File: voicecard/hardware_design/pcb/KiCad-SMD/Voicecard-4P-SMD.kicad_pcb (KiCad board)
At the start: 2 copper layers, 118.7 x 60.3 mm, 92 parts, among them IC1 TL074P, IC2 LM13700N, IC3 TL072P, IC4 V2164D, IC5 TL072P, IC6 MCP4822, IC7 ATMega328p, Q1 2N3906, Q2 2N3906, Q3 20MHz

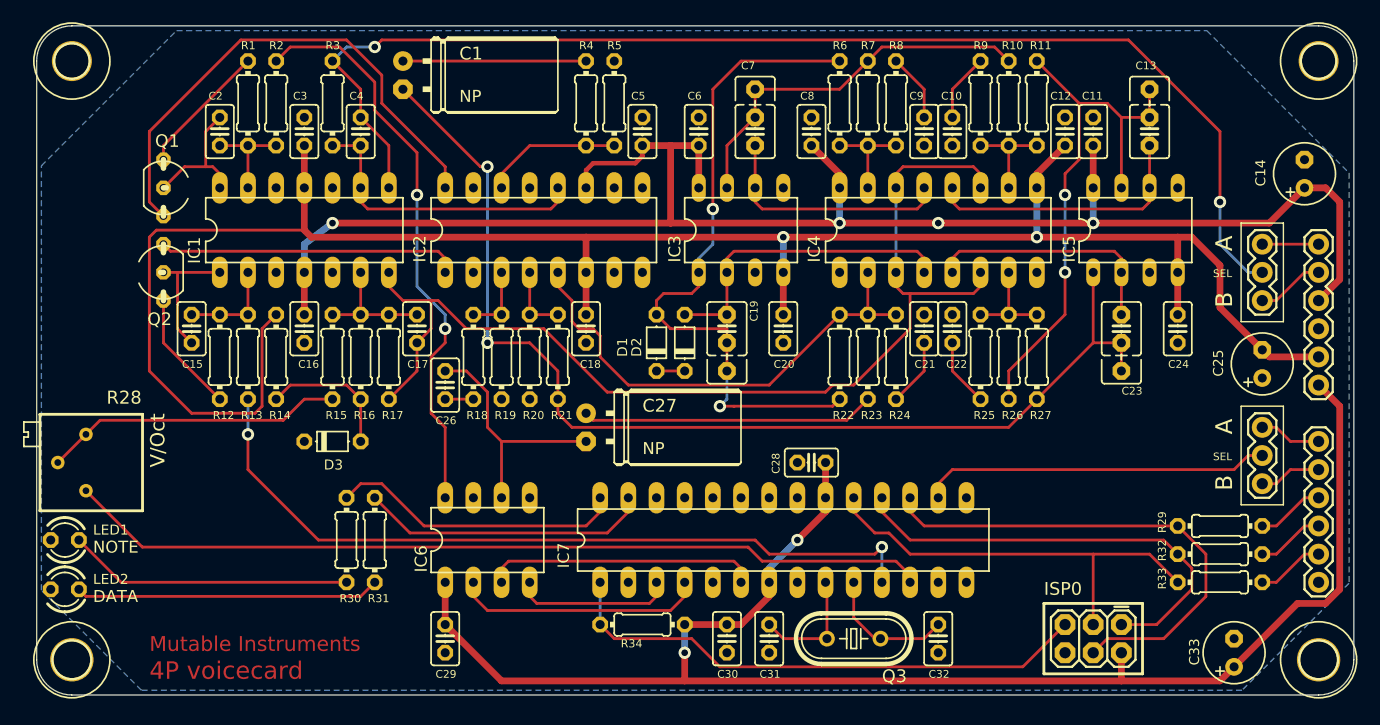
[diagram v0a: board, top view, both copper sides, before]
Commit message: Voicecard 4P SMD: update the board from the schematic and prepare for placement
Footprints replaced in place: every footprint now the schematic's SMD one,
sitting at its through-hole predecessor's position, orientation and layer,
keeping its schematic path. kicad-cli has no update-from-schematic command and
pcbnew does not wrap BOARD_NETLIST_UPDATER, so this was done explicitly
through pcbnew and then checked against the schematic netlist: 92 footprints
(81 replaced, 5 board-only, 6 kept through-hole), 277 of 277 pad nets matching
with nothing extra or missing, and the same net set as the schematic. IC2 pads
7-10 carry no net, being the LM13700 buffer half the 4P does not use.

All 445 track segments, including 20 vias, and the single GND zone are gone.
The Edge.Cuts outline, the four mounting holes, JP1-JP4 and ISP0 are locked:
the motherboard fixes them.

Design rules set to JLCPCB 2-layer standard in the project file: 0.127 mm
minimum track and clearance, 0.3 mm minimum via drill, 0.6 mm minimum via
diameter. Net classes: Default at 0.2 mm track, and a new Power class at
0.4 mm carrying +5V, VCC, VEE and GND. The .kicad_pro is JSON and was edited
with the json module.

DRC reports 196 unconnected items, which is the point of this state, plus one
copper_edge_clearance error where C33's pad crosses the board edge because the
6.3 mm electrolytic sits where a smaller can sat; it goes when C33 is placed.
The 57 warnings are silkscreen and text-height noise inherited from the Eagle
import, along with 4 library mismatches on the imported mounting holes; the
untouched KiCad/ baseline reports 205 violations of the same kinds.

Nothing is placed and nothing is routed.

Co-Authored-By: Claude Opus 5 (1M context) <noreply@anthropic.com>
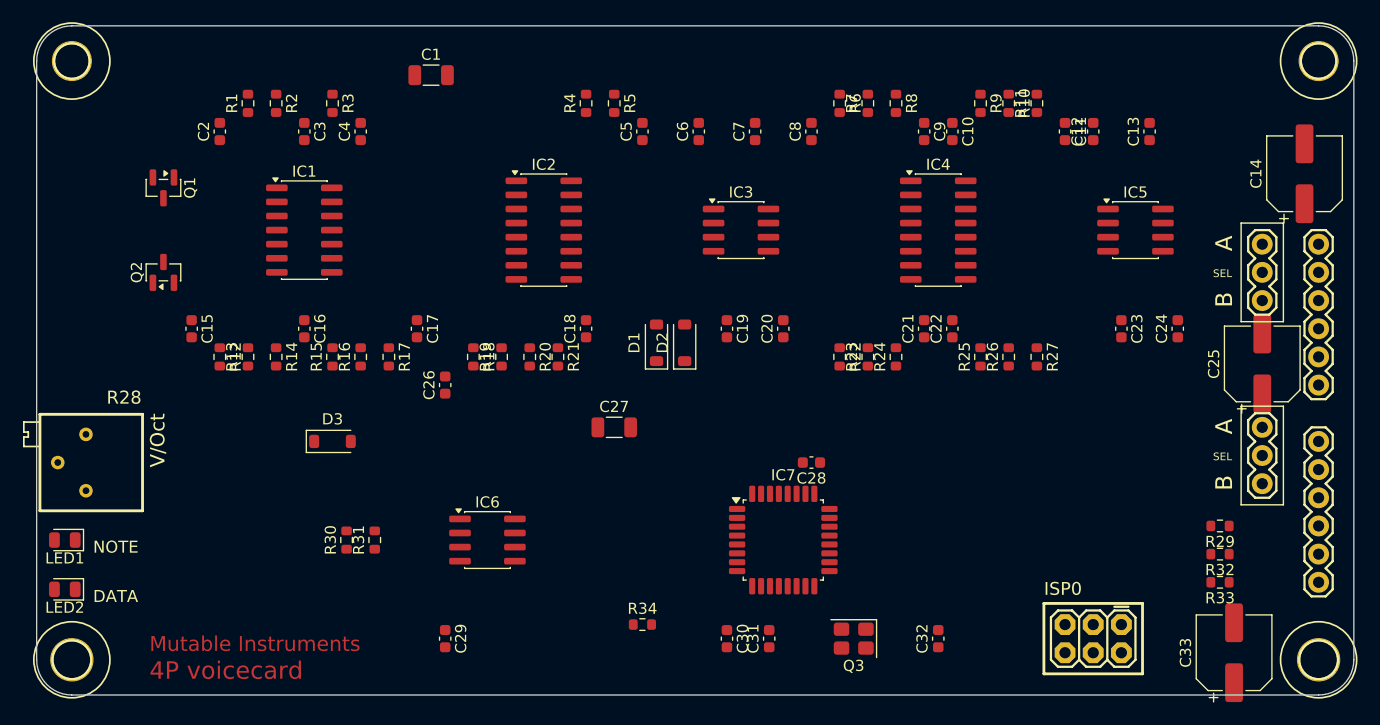
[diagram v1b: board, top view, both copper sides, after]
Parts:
- C1, C27: footprint Voicecard-4P-v01-import-fps:ENP11-6.3 -> Capacitor_SMD:C_1206_3216Metric
- C10, C11, C12, C15, C16, C17, C18, C2, C20, C21, C22, C24, C26, C28, C29, C3, C30, C31, C32, C4, C5, C6, C8, C9: footprint Voicecard-4P-v01-import-fps:C025-025X050 -> Capacitor_SMD:C_0603_1608Metric
- C13, C19, C23, C7: footprint Voicecard-4P-v01-import-fps:C2.5_5-4 -> Capacitor_SMD:C_0603_1608Metric
- C14, C25, C33: footprint Voicecard-4P-v01-import-fps:E2,5-6 -> Capacitor_SMD:CP_Elec_6.3x7.7
- D1, D2, D3: footprint Voicecard-4P-v01-import-fps:D-5 -> Diode_SMD:D_SOD-123
- IC1: footprint Voicecard-4P-v01-import-fps:DIL14 -> Package_SO:SOIC-14_3.9x8.7mm_P1.27mm
- IC2, IC4: footprint Voicecard-4P-v01-import-fps:DIL16 -> Package_SO:SOIC-16_3.9x9.9mm_P1.27mm
- IC3, IC5, IC6: footprint Voicecard-4P-v01-import-fps:DIL08 -> Package_SO:SOIC-8_3.9x4.9mm_P1.27mm
- IC7: footprint Voicecard-4P-v01-import-fps:DIL28-3 -> Package_QFP:TQFP-32_7x7mm_P0.8mm
- LED1, LED2: footprint Voicecard-4P-v01-import-fps:LED3MM -> LED_SMD:LED_0805_2012Metric
- Q1, Q2: footprint Voicecard-4P-v01-import-fps:TO92- -> Package_TO_SOT_SMD:SOT-23
- Q3: footprint Voicecard-4P-v01-import-fps:HC49U-V -> Crystal:Crystal_SMD_3225-4Pin_3.2x2.5mm
- R1, R10, R11, R12, R13, R14, R15, R16, R17, R18, R19, R2, R20, R21, R22, R23, R24, R25, R26, R27, R29, R3, R30, R31, R32, R33, R34, R4, R5, R6, R7, R8, R9: footprint Voicecard-4P-v01-import-fps:0204_7 -> Resistor_SMD:R_0603_1608Metric
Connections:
- C19 pad 1: Net-(IC3A--IN) -> Net-(D2-A)
- IC3 pad 2: Net-(IC3A--IN) -> Net-(D2-A)
- IC4 pad 4: Net-(IC3A--IN) -> Net-(D2-A)
- IC7 pad 1: Net-(IC7-PC6(/RESET)) -> unconnected-(IC7-PD3(INT1)-Pad1)
- IC7 pad 10: Net-(IC7-PB7(XTAL2/TOSC2)) -> F_PWM
- IC7 pad 11: RES_PWM -> unconnected-(IC7-PD7(AIN1)-Pad11)
- IC7 pad 12: F_PWM -> unconnected-(IC7-PB0(ICP)-Pad12)
- IC7 pad 14: unconnected-(IC7-PB0(ICP)-Pad14) -> SS
- IC7 pad 15: unconnected-(IC7-PB1(OC1A)-Pad15) -> MOSI
- IC7 pad 16: SS -> MISO
- IC7 pad 17: MOSI -> SCK
- IC7 pad 18: MISO -> +5V
- IC7 pad 19: SCK -> unconnected-(IC7-ADC6-Pad19)
- IC7 pad 2: unconnected-(IC7-PD0(RXD)-Pad2) -> Net-(IC6-SCK)
- IC7 pad 20: +5V -> unconnected-(IC7-AREF-Pad20)
- IC7 pad 21: unconnected-(IC7-AREF-Pad21) -> GND
- IC7 pad 22: GND -> unconnected-(IC7-ADC7-Pad22)
- IC7 pad 3: Net-(IC6-SDI) -> GND
- IC7 pad 4: Net-(IC6-#CS) -> +5V
- IC7 pad 5: unconnected-(IC7-PD3(INT1)-Pad5) -> GND
- IC7 pad 6: Net-(IC6-SCK) -> +5V
- IC7 pad 7: +5V -> Net-(IC7-PB6(XTAL1/TOSC1))
- IC7 pad 8: GND -> Net-(IC7-PB7(XTAL2/TOSC2))
- IC7 pad 9: Net-(IC7-PB6(XTAL1/TOSC1)) -> RES_PWM
- Q1 pad 1: I_GAIN -> Net-(IC1D-OUT)
- Q1 pad 2: Net-(IC1D-OUT) -> Net-(Q1-E)
- Q1 pad 3: Net-(Q1-E) -> I_GAIN
- Q2 pad 1: I_RESO -> Net-(IC1A-OUT)
- Q2 pad 2: Net-(IC1A-OUT) -> Net-(Q2-E)
- Q2 pad 3: Net-(Q2-E) -> I_RESO
- Q3 pad 2: Net-(IC7-PB6(XTAL1/TOSC1)) -> GND
- R14 pad 2: Net-(D3-PadA) -> Net-(D3-A)
- R16 pad 1: Net-(D3-PadA) -> Net-(D3-A)
- R23 pad 1: Net-(C27-1) -> Net-(C27-Pad1)
- R30 pad 1: Net-(LED1-PadA) -> Net-(LED1-A)
- R31 pad 1: Net-(LED2-PadA) -> Net-(LED2-A)
- R4 pad 2: Net-(C1-1) -> Net-(C1-Pad1)
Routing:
- net VEE: track 183.4 -> 0.00 mm, vias 2 -> 0
- net VCC: track 150.9 -> 0.00 mm, vias 4 -> 0
- net +5V: track 139.6 -> 0.00 mm, vias 2 -> 0
- net OUT: track 112.8 -> 0.00 mm, vias 2 -> 0
- net LP4: track 101.0 -> 0.00 mm, vias 2 -> 0
- net F_CV: track 97.2 -> 0.00 mm
- net F_PWM: track 78.1 -> 0.00 mm
- net RES_PWM: track 70.1 -> 0.00 mm, vias 2 -> 0
- net LP1: track 61.6 -> 0.00 mm, vias 2 -> 0
- net VCA_CONTROL: track 51.9 -> 0.00 mm, vias 2 -> 0
- net LP3: track 50.5 -> 0.00 mm, vias 2 -> 0
- net Net-(IC7-PC6(/RESET)): track 48.9 -> 0.00 mm
- net I_GAIN: track 46.4 -> 0.00 mm
- net MOSI: track 45.6 -> 0.00 mm
- net Net-(IC2C-OUT): track 44.1 -> 0.00 mm
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- removed copper zone on B.Cu, net GND

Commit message: Voicecard 4P SMD: light placement pass, nothing routed
Olivier's arrangement is kept; nothing compacted or regrouped. Locked parts
(connectors, mounting holes, outline) did not move.

Decoupling was the real finding: every 100n sat 5.97 to 13.99 mm from the
supply pins it serves, because the SOIC and TQFP bodies are so much smaller
than the DIPs they replaced. Each cap now sits beside its IC's supply pad,
assigned to minimise total travel, at 0.88 to 2.88 mm.

The crystal loop closed up: Q3, C31 and C32 moved from 10-17 mm away to sit
against IC7's XTAL pins, terminals now 1.65 mm (XTAL2) and 3.35 mm (XTAL1)
from the MCU with the load caps flanking the crystal. The 3225's terminals are
diagonally opposite, so one is always the far one whichever way it is turned.

C33 moved out of the bottom-right corner, where its pad crossed the board
edge. It could not simply move inboard: the U$5 mounting hole, ISP0, R33 and
JP4 box that corner in and the 9.5 mm can does not fit between them, so it
went to the free band at (191.5, 113.5), still on the connector side.

Q1 and Q2 are NOT an expo pair, so they were left alone. Each is a separate
op-amp servo current source: Q1's base from IC1D with R1 emitter feedback,
collector to I_GAIN; Q2 the same around IC1A with R12, collector to I_RESO.
They share no node. The V/Oct exponential conversion is internal to the
SSI2164, driven from F_CV via IC1B with R28 setting the scale through R15.

All unlocked footprints are on a 0.5 mm grid except C25, which has 0.06 mm of
slack between JP1 and JP3 and keeps its imported position rather than being
nudged into a locked connector. 24 0603 orientations were normalised to their
own axis, so each group agrees without any pad moving.

DRC: copper_edge_clearance is zero and there are no courtyard overlaps. 196
unconnected items remain, as they should with no track laid. Silkscreen
warnings rose from 57 to 82 now that parts are closer; that belongs to the
silkscreen pass after routing.

Co-Authored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
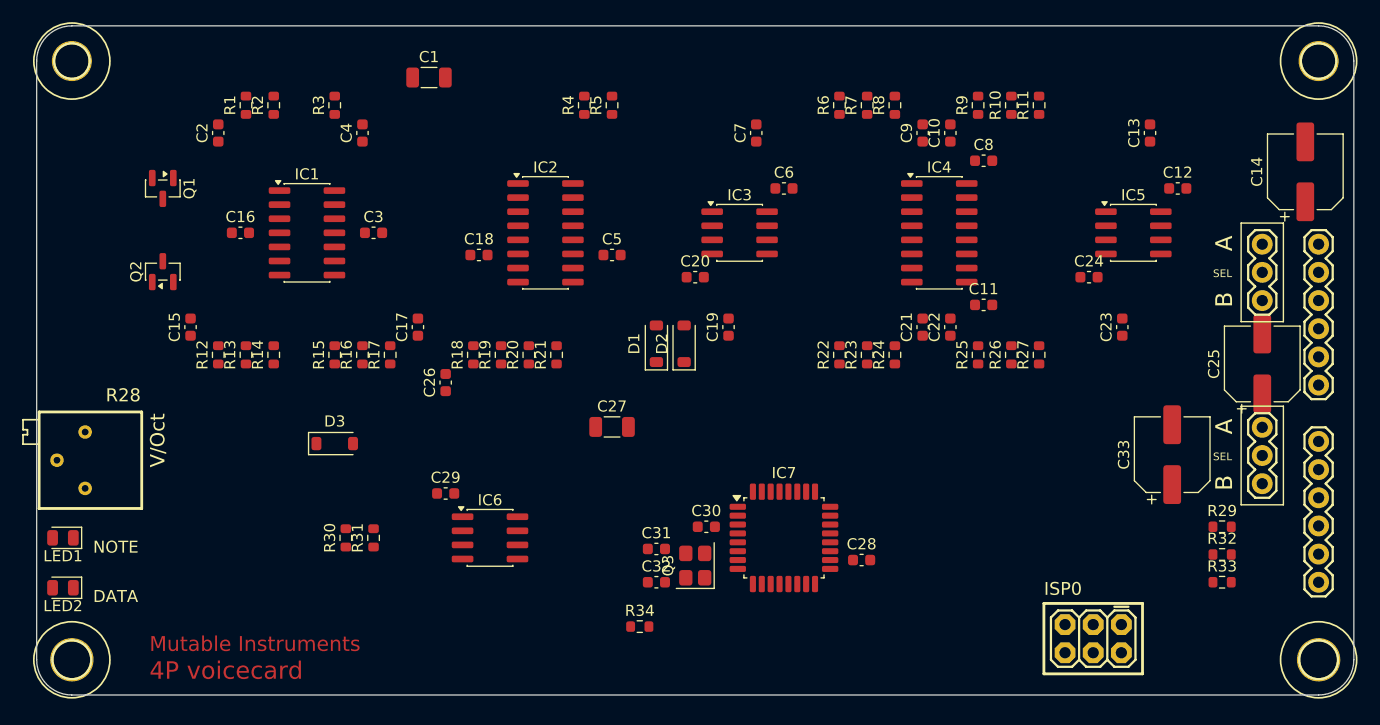
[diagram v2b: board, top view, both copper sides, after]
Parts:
- moved C32 25.9 mm to (145.0, 125.0), turned to 0 degrees
- moved C33 18.7 mm to (191.5, 113.5)
- moved C11 17.3 mm to (174.5, 100.0), turned to 0 degrees
- moved C8 15.7 mm to (174.5, 87.0), turned to 0 degrees
- moved Q3 15.7 mm to (148.5, 123.5), turned to 90 degrees
- moved C29 13.1 mm to (126.0, 117.0), turned to 0 degrees
- moved C31 13.0 mm to (145.0, 122.0), turned to 0 degrees
- moved C18 11.7 mm to (129.0, 95.5), turned to 0 degrees
- moved C5 11.5 mm to (141.0, 95.5), turned to 0 degrees
- moved C3 11.1 mm to (119.5, 93.5), turned to 0 degrees
- moved C16 10.4 mm to (107.5, 93.5), turned to 0 degrees
- moved C30 10.3 mm to (149.5, 120.0), turned to 0 degrees
- moved C28 9.88 mm to (163.5, 123.0), turned to 0 degrees
- moved C24 9.25 mm to (184.0, 97.5), turned to 0 degrees
- moved C6 9.24 mm to (156.5, 89.5), turned to 0 degrees
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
